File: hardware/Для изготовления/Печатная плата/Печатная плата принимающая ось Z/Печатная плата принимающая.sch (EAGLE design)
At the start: 6 parts, among them J1 22-03-5035, X1 0446200001

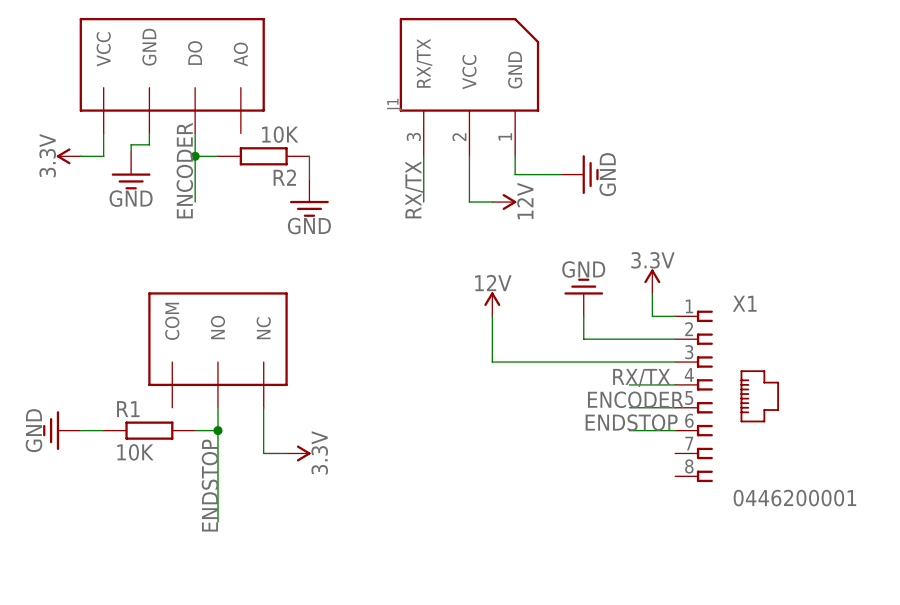
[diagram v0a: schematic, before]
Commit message: Изменена плата принимающая под  ось Z
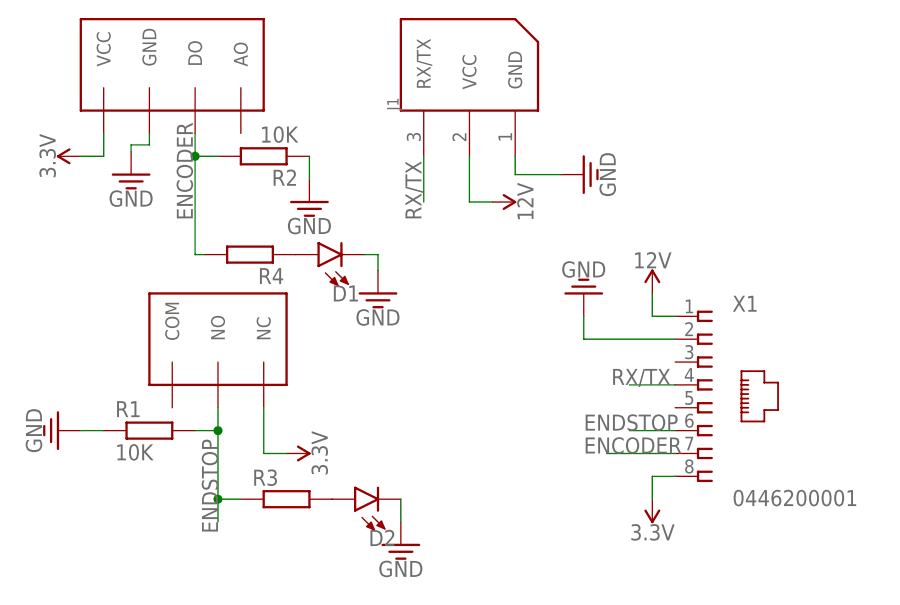
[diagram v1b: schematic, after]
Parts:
- added D1, D2: (no value), SparkFun-LED:LED5MM
- added R3, R4: (no value), resistor:R-EU_0204/7
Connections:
- new net N$1: D2.A, R3.2
- new net N$2: D1.A, R4.1
- net 12V: now also X1.1; no longer X1.3
- net 3.3V: now also X1.8; no longer X1.1
- net ENCODER: now also R4.2, X1.7; no longer X1.5
- net ENDSTOP: now also R3.1
- net GND: now also D1.C, D2.C
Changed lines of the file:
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@@
 <layer number="230" name="230bmp" color="7" fill="1" visible="yes" active="yes"/>
 <layer number="231" name="231bmp" color="7" fill="1" visible="yes" active="yes"/>
+<layer number="232" name="Eagle3D_PG2" color="7" fill="1" visible="yes" active="yes"/>
+<layer number="233" name="Eagle3D_PG3" color="7" fill="1" visible="yes" active="yes"/>
 <layer number="248" name="Housing" color="7" fill="1" visible="yes" active="yes"/>
 <layer number="249" name="Edge" color="7" fill="1" visible="yes" active="yes"/>
@@
 <part name="GND5" library="SparkFun-PowerSymbols" deviceset="GND2" device="" value="GND"/>
 <part name="X1" library="con-molex" library_urn="urn:adsk.eagle:library:165" deviceset="0446200001" device=""/>
+<part name="D1" library="SparkFun-LED" deviceset="LED" device="5MM"/>
+<part name="D2" library="SparkFun-LED" deviceset="LED" device="5MM"/>
+<part name="R3" library="resistor" library_urn="urn:adsk.eagle:library:348" deviceset="R-EU_" device="0204/7" package3d_urn="urn:adsk.eagle:package:25945/1"/>
+<part name="R4" library="resistor" library_urn="urn:adsk.eagle:library:348" deviceset="R-EU_" device="0204/7" package3d_urn="urn:adsk.eagle:package:25945/1"/>
+<part name="GND6" library="SparkFun-PowerSymbols" deviceset="GND2" device="" value="GND"/>
+<part name="GND7" library="SparkFun-PowerSymbols" deviceset="GND2" device="" value="GND"/>
 </parts>
 <sheets>
@@
 <instance part="J1" gate="G$1" x="71.12" y="83.82" rot="R90"/>
 <instance part="SUPPLY1" gate="G$1" x="27.94" y="73.66" rot="R90"/>
-<instance part="SUPPLY2" gate="G$1" x="91.44" y="58.42"/>
+<instance part="SUPPLY2" gate="G$1" x="91.44" y="35.56" rot="R180"/>
 <instance part="SUPPLY3" gate="G$1" x="73.66" y="68.58" rot="R270"/>
 <instance part="GND1" gate="GND" x="33.528" y="71.628"/>
 <instance part="GND2" gate="GND" x="83.82" y="71.628" rot="R90"/>
 <instance part="GND3" gate="GND" x="83.82" y="58.42" rot="R180"/>
-<instance part="SUPPLY4" gate="G$1" x="73.66" y="55.88"/>
+<instance part="SUPPLY4" gate="G$1" x="91.44" y="58.42"/>
 <instance part="U$2" gate="G$1" x="43.18" y="53.34"/>
 <instance part="SUPPLY5" gate="G$1" x="50.8" y="40.64" rot="R270"/>
@@
 <instance part="GND5" gate="GND" x="53.34" y="68.58"/>
 <instance part="X1" gate="P" x="96.52" y="45.72"/>
+<instance part="D1" gate="G$1" x="54.356" y="62.738" rot="R90"/>
+<instance part="D2" gate="G$1" x="58.42" y="35.56" rot="R90"/>
+<instance part="R3" gate="G$1" x="50.8" y="35.56"/>
+<instance part="R4" gate="G$1" x="46.736" y="62.738" rot="R180"/>
+<instance part="GND6" gate="GND" x="63.5" y="30.48"/>
+<instance part="GND7" gate="GND" x="60.96" y="58.42"/>
 </instances>
 <busses>
@@
 <segment>
 <pinref part="SUPPLY4" gate="G$1" pin="12V"/>
-<wire x1="73.66" y1="55.88" x2="73.66" y2="50.8" width="0.1524" layer="91"/>
-<wire x1="73.66" y1="50.8" x2="93.98" y2="50.8" width="0.1524" layer="91"/>
-<pinref part="X1" gate="P" pin="3"/>
+<pinref part="X1" gate="P" pin="1"/>
+<wire x1="91.44" y1="58.42" x2="91.44" y2="55.88" width="0.1524" layer="91"/>
+<wire x1="91.44" y1="55.88" x2="93.98" y2="55.88" width="0.1524" layer="91"/>
 </segment>
 </net>
@@
 </segment>
 <segment>
-<pinref part="SUPPLY2" gate="G$1" pin="3.3V"/>
-<wire x1="91.44" y1="58.42" x2="91.44" y2="55.88" width="0.1524" layer="91"/>
-<wire x1="91.44" y1="55.88" x2="93.98" y2="55.88" width="0.1524" layer="91"/>
-<pinref part="X1" gate="P" pin="1"/>
-</segment>
-<segment>
 <pinref part="U$2" gate="G$1" pin="NC"/>
 <wire x1="48.26" y1="45.72" x2="48.26" y2="40.64" width="0.1524" layer="91"/>
 <pinref part="SUPPLY5" gate="G$1" pin="3.3V"/>
 <wire x1="48.26" y1="40.64" x2="50.8" y2="40.64" width="0.1524" layer="91"/>
+</segment>
+<segment>
+<pinref part="X1" gate="P" pin="8"/>
+<pinref part="SUPPLY2" gate="G$1" pin="3.3V"/>
+<wire x1="93.98" y1="38.1" x2="91.44" y2="38.1" width="0.1524" layer="91"/>
+<wire x1="91.44" y1="38.1" x2="91.44" y2="35.56" width="0.1524" layer="91"/>
 </segment>
 </net>
@@
 <wire x1="53.34" y1="71.12" x2="53.34" y2="73.66" width="0.1524" layer="91"/>
 </segment>
+<segment>
+<pinref part="D2" gate="G$1" pin="C"/>
+<pinref part="GND6" gate="GND" pin="GND"/>
+<wire x1="63.5" y1="35.56" x2="63.5" y2="33.02" width="0.1524" layer="91"/>
+</segment>
+<segment>
+<pinref part="D1" gate="G$1" pin="C"/>
+<pinref part="GND7" gate="GND" pin="GND"/>
+<wire x1="59.436" y1="62.738" x2="60.96" y2="62.738" width="0.1524" layer="91"/>
+<wire x1="60.96" y1="62.738" x2="60.96" y2="60.96" width="0.1524" layer="91"/>
+</segment>
 </net>
 <net name="RX/TX" class="0">
@@
 </net>
 <net name="ENCODER" class="0">
-<segment>
-<wire x1="93.98" y1="45.72" x2="88.9" y2="45.72" width="0.1524" layer="91"/>
-<label x="84.074" y="45.72" size="1.778" layer="95"/>
-<pinref part="X1" gate="P" pin="5"/>
-</segment>
 <segment>
 <pinref part="U$1" gate="G$1" pin="DO"/>
@@
 <label x="40.386" y="66.548" size="1.778" layer="95" rot="R90"/>
 <pinref part="R2" gate="G$1" pin="2"/>
-<wire x1="40.64" y1="73.66" x2="40.64" y2="68.58" width="0.1524" layer="91"/>
 <wire x1="43.18" y1="73.66" x2="40.64" y2="73.66" width="0.1524" layer="91"/>
 <junction x="40.64" y="73.66"/>
+<wire x1="40.64" y1="73.66" x2="40.64" y2="62.738" width="0.1524" layer="91"/>
+<pinref part="R4" gate="G$1" pin="2"/>
+<wire x1="40.64" y1="62.738" x2="41.656" y2="62.738" width="0.1524" layer="91"/>
+</segment>
+<segment>
+<pinref part="X1" gate="P" pin="7"/>
+<wire x1="93.98" y1="40.64" x2="86.36" y2="40.64" width="0.1524" layer="91"/>
+<label x="83.82" y="40.64" size="1.778" layer="95"/>
 </segment>
 </net>
@@
 <wire x1="40.64" y1="43.18" x2="43.18" y2="43.18" width="0.1524" layer="91"/>
 <junction x="43.18" y="43.18"/>
-<wire x1="43.18" y1="43.18" x2="43.18" y2="33.02" width="0.1524" layer="91"/>
+<wire x1="43.18" y1="43.18" x2="43.18" y2="35.56" width="0.1524" layer="91"/>
 <label x="43.18" y="31.75" size="1.778" layer="95" rot="R90"/>
-</segment>
-</net>
+<pinref part="R3" gate="G$1" pin="1"/>
+<wire x1="43.18" y1="35.56" x2="43.18" y2="33.02" width="0.1524" layer="91"/>
+<wire x1="43.18" y1="35.56" x2="45.72" y2="35.56" width="0.1524" layer="91"/>
+<junction x="43.18" y="35.56"/>
+</segment>
+</net>
+<net name="N$1" class="0">
+<segment>
+<pinref part="R3" gate="G$1" pin="2"/>
+<pinref part="D2" gate="G$1" pin="A"/>
+</segment>
+</net>
+<net name="N$2" class="0">
+<segment>
+<pinref part="R4" gate="G$1" pin="1"/>
+<pinref part="D1" gate="G$1" pin="A"/>
+</segment>
+</net>
